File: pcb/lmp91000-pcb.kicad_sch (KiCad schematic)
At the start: 17 parts, among them J1 TC2030, U1 2450AT18D0100001E, U2 EFR32BG24L210F768IM40-B, Y1 XTL501250-S315-038

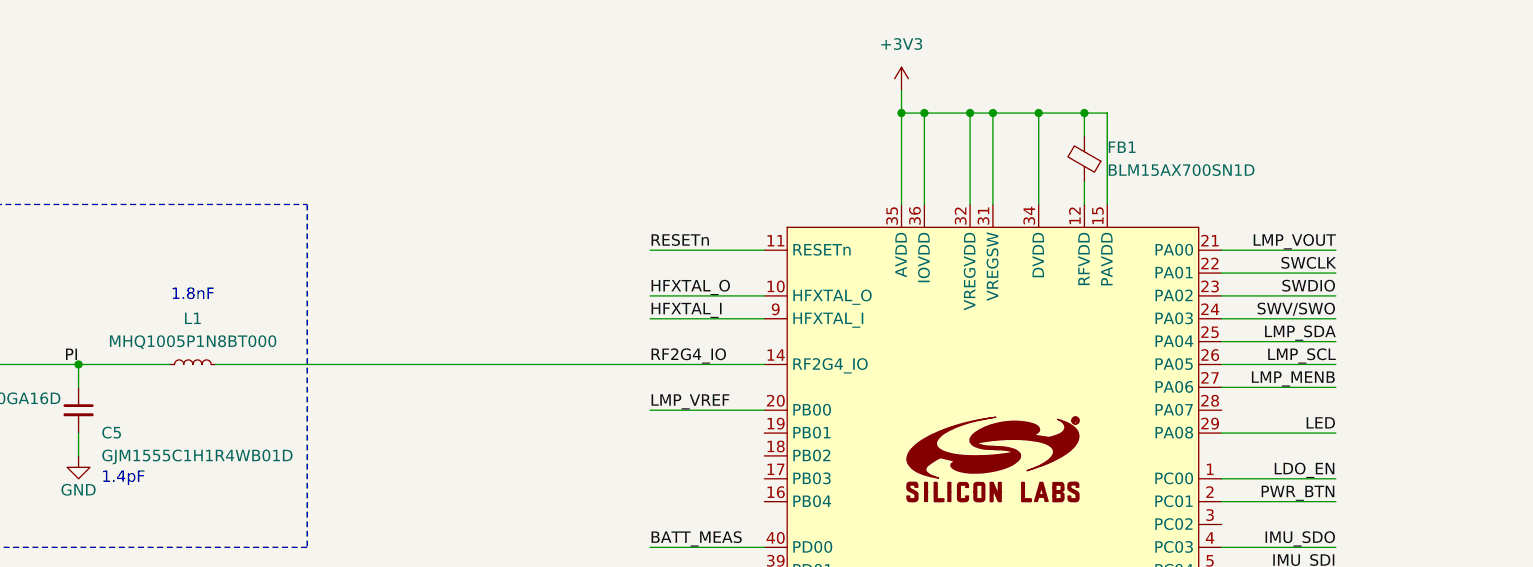
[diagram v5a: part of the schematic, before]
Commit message: Create Simplicity Studio 6 firmware project
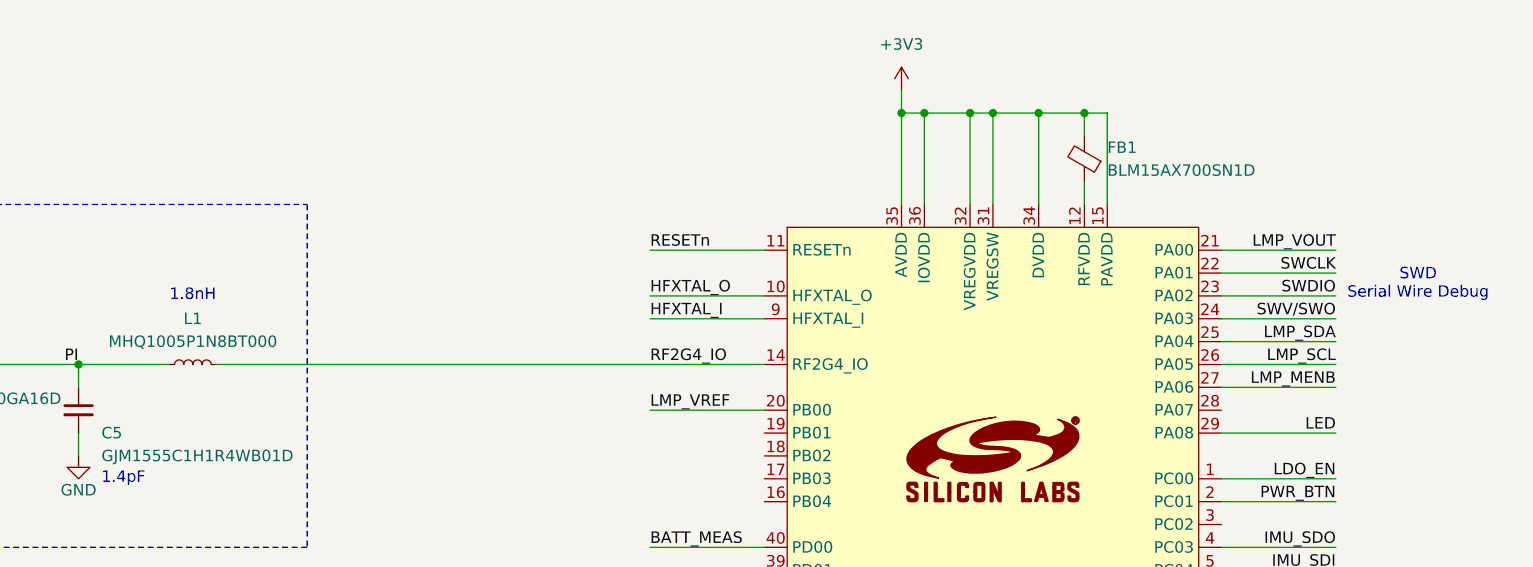
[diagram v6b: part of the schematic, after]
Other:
- note added: "1.8nH"
- note added: "SWD Serial Wire Debug"
- note removed: "1.8nF"
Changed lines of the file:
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@@
 		)
 	)
-	(text "1.8nF"
+	(text "1.8nH"
 		(exclude_from_sim no)
 		(at 139.7 99.06 0)
@@
 		)
 	)
+	(text "SWD\nSerial Wire Debug"
+		(exclude_from_sim no)
+		(at 275.844 97.79 0)
+		(effects
+			(font
+				(size 1.27 1.27)
+			)
+		)
+	)
